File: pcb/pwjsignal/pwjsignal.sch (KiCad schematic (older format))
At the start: 68 parts, among them J1 Strain Gauge, J10 CN10, J11 microSD_SDIO, J2 NUCLEO E5V, J3 Power In, J4 microSD, J5 CONN_LEDPWR, J6 CONN_LEDPWR, J7 CN7, J8 CN8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

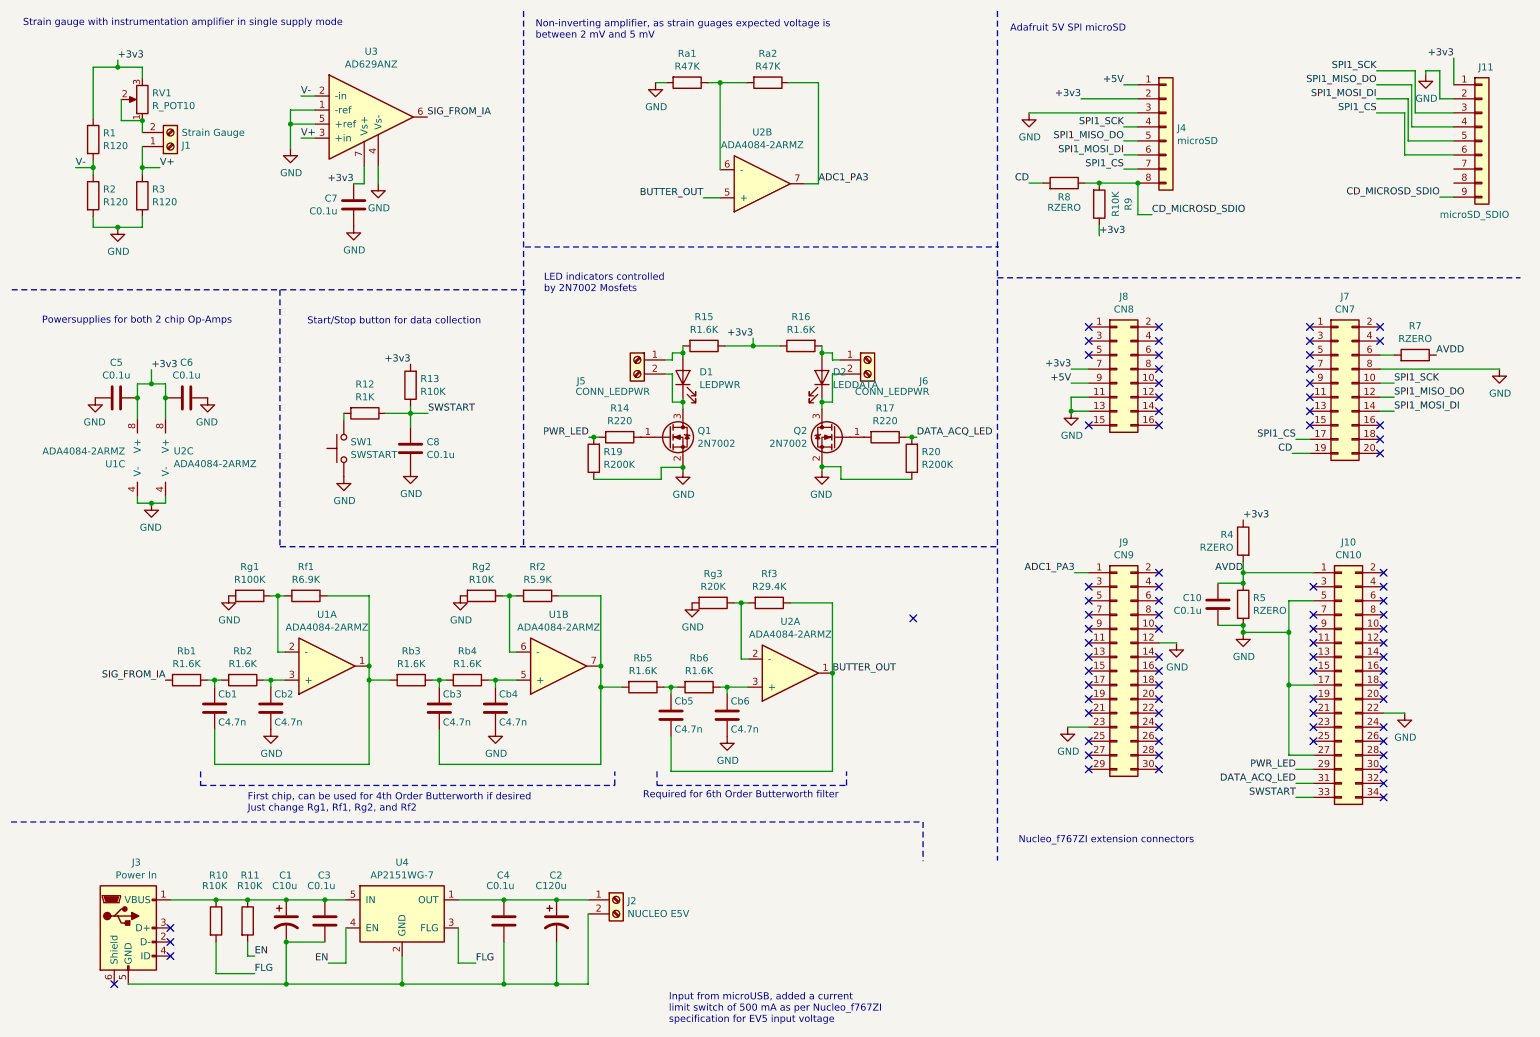
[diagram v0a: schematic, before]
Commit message: Added Rev B of board with updated filters
* This includes new Low Pass filter cutoff frequency 80kHz.
* New instrumentation amplifier for low noise
* Added test points
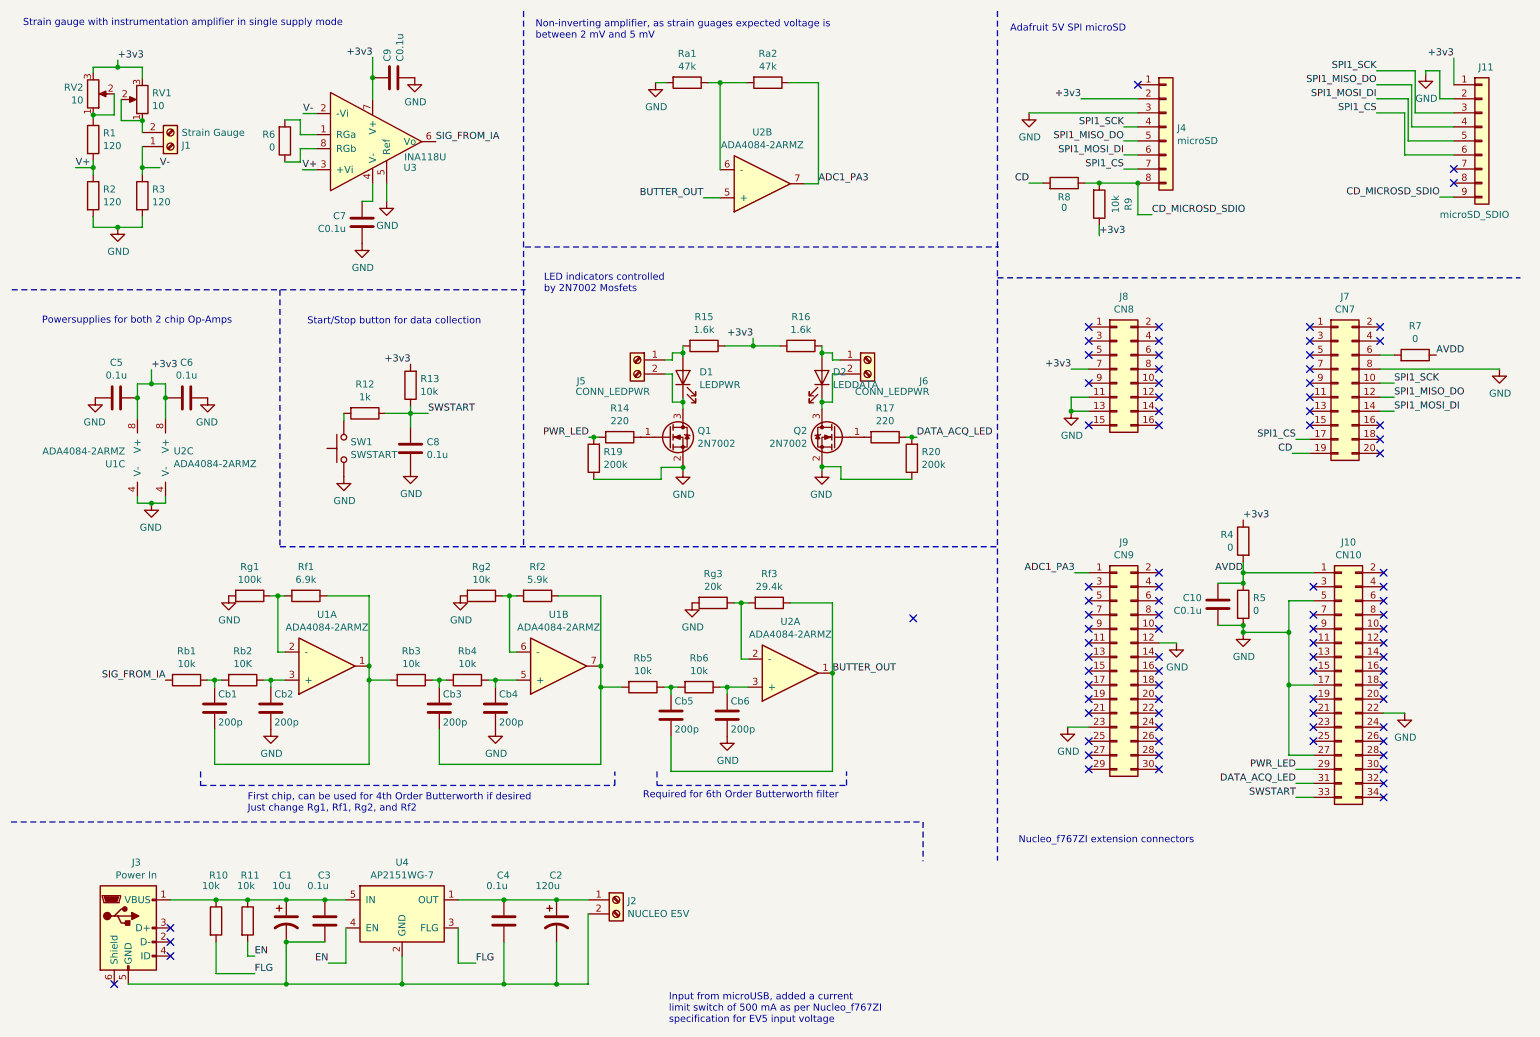
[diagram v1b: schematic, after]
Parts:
- removed U3: AD629ANZ, Package_SO:SOIC-8_3.9x4.9mm_P1.27mm, symbol Personal:AD629ANZ
- added C9: C0.1u, Capacitor_SMD:C_1206_3216Metric_Pad1.42x1.75mm_HandSolder, symbol Device:C
- added R6: 0, Resistor_SMD:R_0603_1608Metric_Pad1.05x0.95mm_HandSolder, symbol Device:R
- added RV2: 10, Potentiometer_SMD:Potentiometer_Bourns_3214J_Horizontal, symbol Device:R_POT
- added U3: INA118U, Package_SO:SOIC-8_3.9x4.9mm_P1.27mm, symbol Personal:INA118U
- C1: value C10u -> 10u
- C2: value C120u -> 120u
- C3, C4, C5, C6, C8: value C0.1u -> 0.1u
- Cb1, Cb2, Cb3, Cb4, Cb5, Cb6: value C4.7n -> 200p
- R1, R2, R3: value R120 -> 120
- R10, R11, R13, R9, Rg2: value R10K -> 10k
- R12: value R1K -> 1k
- R14, R17: value R220 -> 220
- R15, R16: value R1.6K -> 1.6k
- R19, R20: value R200K -> 200k
- R4, R5, R7, R8: value RZERO -> 0
- RV1: value R_POT10 -> 10
- Ra1, Ra2: value R47K -> 47k
- Rb1, Rb3, Rb4, Rb5, Rb6: value R1.6K -> 10k
- Rb2: value R1.6K -> 10K
- Rf1: value R6.9K -> 6.9k
- Rf2: value R5.9K -> 5.9k
- Rf3: value R29.4K -> 29.4k
- Rg1: value R100K -> 100k
- Rg3: value R20K -> 20k
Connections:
- net +3v3: now also C9.2, RV2.3, U3.7 (V+); no longer C7.2, R1.1
- net GND: now also C9.1, U3.5 (Ref)
- net SIG_FROM_IA: now also U3.6 (Vo)
- net V+: now also R1.2, R2.1, U3.3 (+Vi); no longer J1.1 (Pin_1), R3.1
- net V-: now also J1.1 (Pin_1), R3.1, U3.2 (-Vi); no longer R1.2, R2.1
- net +5V: no longer names the net of J4.1 (Pin_1)
- net +5V: no longer J8.9 (Pin_9)
- new net: R1.1, RV2.1, RV2.2
- new net: C7.2, U3.4 (V-)
- new net: R6.2, U3.1 (RGa)
- new net: R6.1, U3.8 (RGb)
- no-connect marks 83 -> 87
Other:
- moved on the sheet: C7
